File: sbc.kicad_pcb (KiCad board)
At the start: 4 copper layers, 90 parts, among them CON1 Micro_SD_Card, IC1 AM335X_ZCZ, P1 USB_A, Y1 32.768KHz, Y2 24MHz

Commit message: Regular backup
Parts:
- C38, C49, C50, C51, R13: moved to B.Cu
- Y1, Y2: footprint Crystals:Crystal_SMD_0603-2pin_6.0x3.5mm_HandSoldering -> Crystals:Crystal_SMD_2012-2pin_2.0x1.2mm_HandSoldering
- moved R13 151.5 mm to (93.0, 55.9)
- moved C46 141.9 mm to (98.6, 76.2)
- moved R14 140.6 mm to (94.7, 78.7)
- moved C50 138.5 mm to (94.5, 62.8)
- moved C48 136.9 mm to (100.0, 56.7)
- moved C28 128.9 mm to (95.6, 56.6)
- moved C51 127.0 mm to (98.3, 59.7)
- moved C49 124.9 mm to (98.6, 61.3)
- moved C47 121.6 mm to (94.6, 77.0)
- moved Y1 104.4 mm to (91.4, 56.6), turned to 180 degrees
- moved C38 104.0 mm to (93.3, 57.9)
- moved F1 95.7 mm to (106.4, 73.2)
- moved Y2 94.8 mm to (94.8, 75.2)
- moved C8 24.1 mm to (163.8, 132.8), turned to 90 degrees
- moved CON1 10.6 mm to (179.0, 105.5)
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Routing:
- net 1.1V: track 30.2 -> 69.8 mm, vias 2 -> 8
- net +3V3: track 0.00 -> 37.2 mm, vias 0 -> 3
- net 1.8V: track 8.80 -> 32.9 mm, vias 0 -> 2
- net +5V: track 24.2 -> 40.9 mm, vias 0 -> 3
- net Net-(C28-Pad1): track 0.00 -> 11.7 mm, vias 0 -> 2
- net Net-(C46-Pad1): track 0.00 -> 10.7 mm
- net Net-(C48-Pad1): track 0.00 -> 10.6 mm, vias 0 -> 2
- net GND_OSC1: track 0.00 -> 9.88 mm, vias 0 -> 2
- net Net-(IC1-PadB4): track 0.00 -> 9.74 mm, vias 0 -> 1
- net /USBD+: track 0.00 -> 9.72 mm
- net /USBD-: track 0.00 -> 9.44 mm
- net GND_OSC0: track 0.00 -> 8.75 mm
- net GND: track 104.9 -> 113.6 mm, vias 36 -> 38
- net Net-(C47-Pad1): track 0.00 -> 6.35 mm
- net Net-(C38-Pad1): track 0.00 -> 5.44 mm, vias 0 -> 1
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
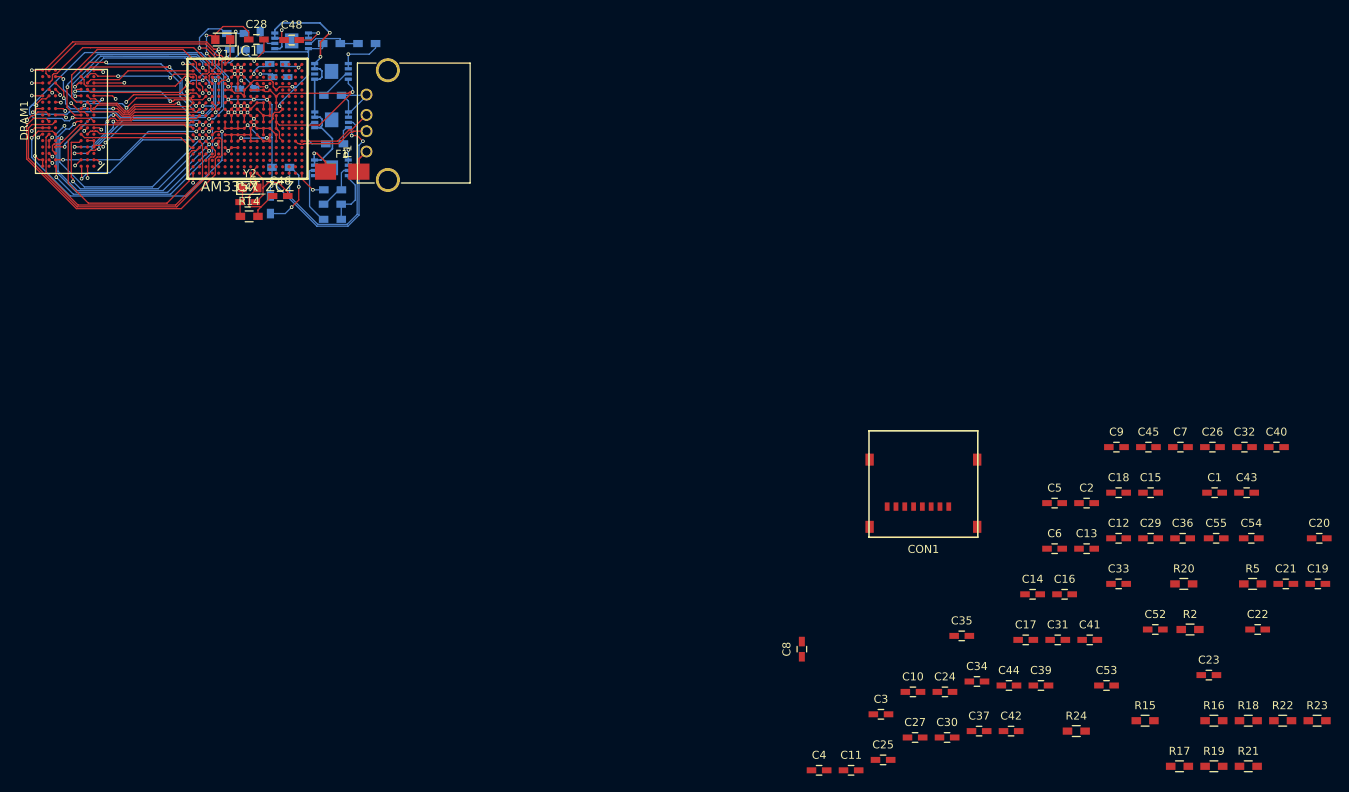
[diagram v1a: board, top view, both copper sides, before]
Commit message: board design v1 almost complete
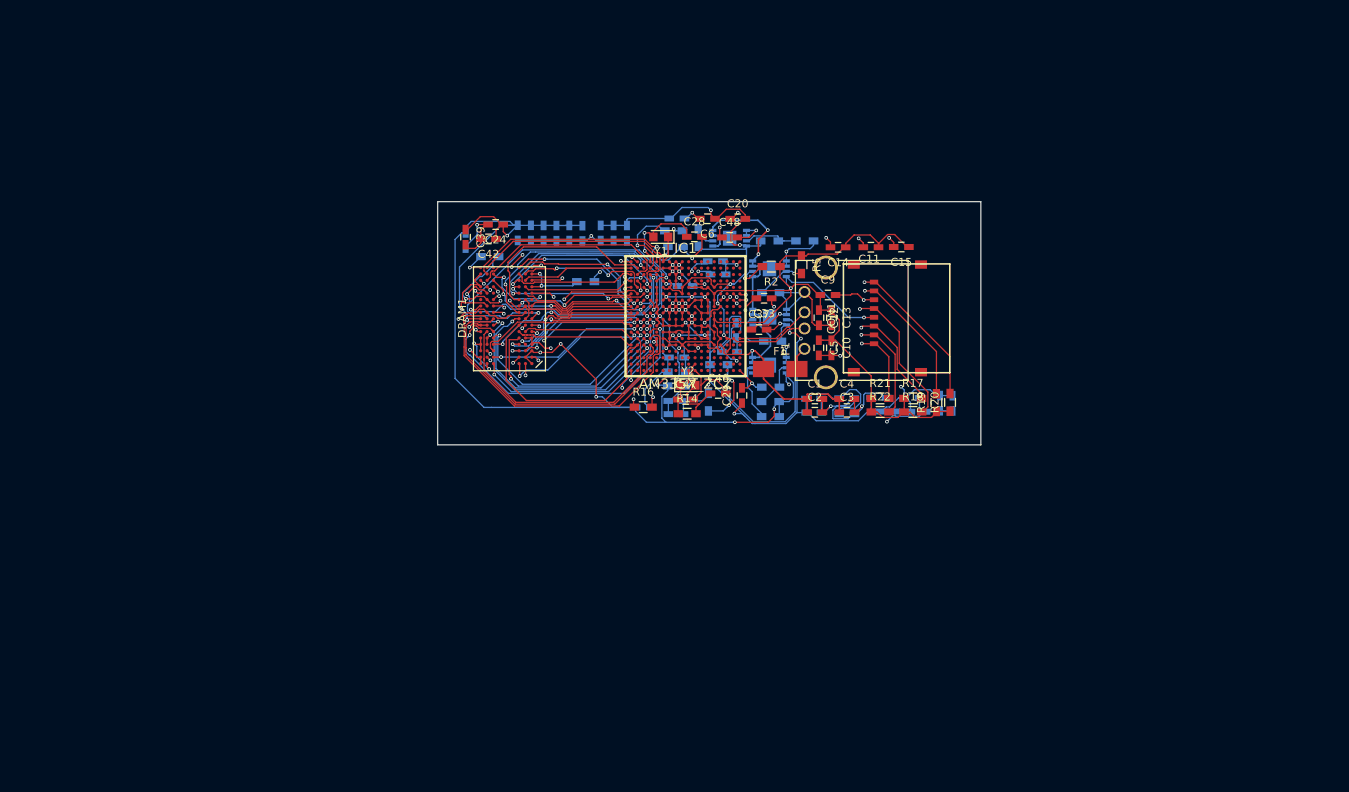
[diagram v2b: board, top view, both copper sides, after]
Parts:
- added R25: 10K, Resistors_SMD:R_0603_HandSoldering, B.Cu at (136.8, 86.9)
- C16, C17, C18, C19, C21, C22, C23, C25, C26, C27, C30, C31, C32, C34, C35, C36, C40, C41, C43, C44, C45, C52, C53, C54, C55, C7, C8, R15, R23, R24: moved to B.Cu
- moved R15 100.4 mm to (124.8, 83.8)
- moved C22 99.3 mm to (134.8, 80.8), turned to 270 degrees
- moved C21 98.2 mm to (136.4, 80.9), turned to 270 degrees
- moved C19 92.2 mm to (148.2, 79.0)
- moved C43 92.2 mm to (133.2, 80.8), turned to 270 degrees
- moved C39 91.2 mm to (121.8, 81.3), turned to 270 degrees
- moved R23 90.3 mm to (148.2, 99.9)
- moved C42 89.7 mm to (124.7, 81.6), turned to 180 degrees
- moved C26 87.8 mm to (131.5, 80.8), turned to 270 degrees
- moved C44 87.8 mm to (121.8, 81.8), turned to 90 degrees
- moved C20 82.9 mm to (155.8, 79.0)
- moved R16 81.4 mm to (144.0, 102.6)
- moved C24 81.0 mm to (125.5, 79.8), turned to 180 degrees
- moved C27 80.3 mm to (128.3, 80.8), turned to 90 degrees
- moved C25 79.2 mm to (130.0, 80.8), turned to 270 degrees
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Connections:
- C15 pad 1: GND -> +3V3
- C15 pad 2: +3V3 -> GND
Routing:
- net +1.5V: track 7.30 -> 254.2 mm, vias 0 -> 23
- net GND: track 113.6 -> 233.2 mm, vias 38 -> 54
- net +3V3: track 37.2 -> 127.3 mm, vias 3 -> 5
- net 1.1V: track 69.8 -> 128.4 mm, vias 8 -> 12
- net 1.8V: track 32.9 -> 82.8 mm, vias 2 -> 7
- net /MMC0_DAT1: track 0.00 -> 39.9 mm, vias 0 -> 2
- net /MMC0_DAT0: track 0.00 -> 37.4 mm, vias 0 -> 2
- net /MMC0_DAT3: track 0.00 -> 34.4 mm, vias 0 -> 2
- net /MMC0_CLK: track 0.00 -> 34.3 mm, vias 0 -> 2
- net /MMC0_CMD: track 0.00 -> 32.0 mm, vias 0 -> 2
- net /MMC0_DAT2: track 0.00 -> 31.9 mm, vias 0 -> 2
- net /DDR_VREF: track 48.1 -> 73.0 mm
- net +5V: track 40.9 -> 61.8 mm
- net Net-(P1-Pad5): track 0.00 -> 20.7 mm
- net Net-(IC1-PadJ3): track 0.00 -> 14.9 mm, vias 0 -> 4
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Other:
- board outline added: 67.9 x 30.4 mm
